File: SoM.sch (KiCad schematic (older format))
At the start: 9 parts

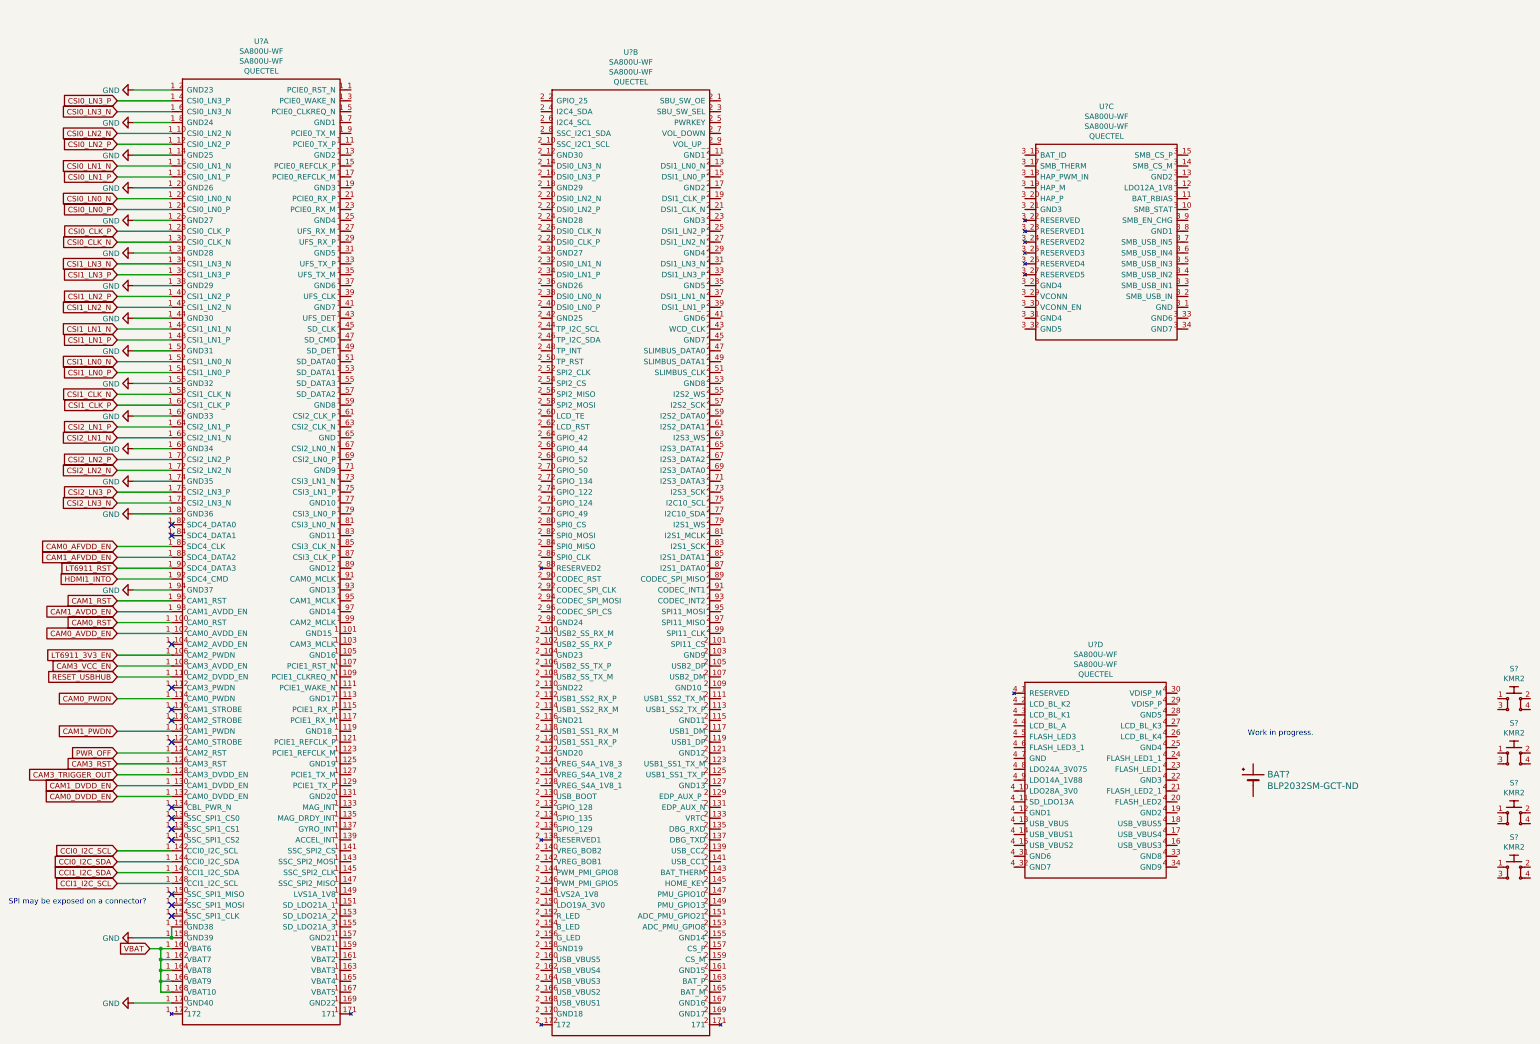
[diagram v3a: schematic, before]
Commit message: added components to pcb and fixed corresponding errors
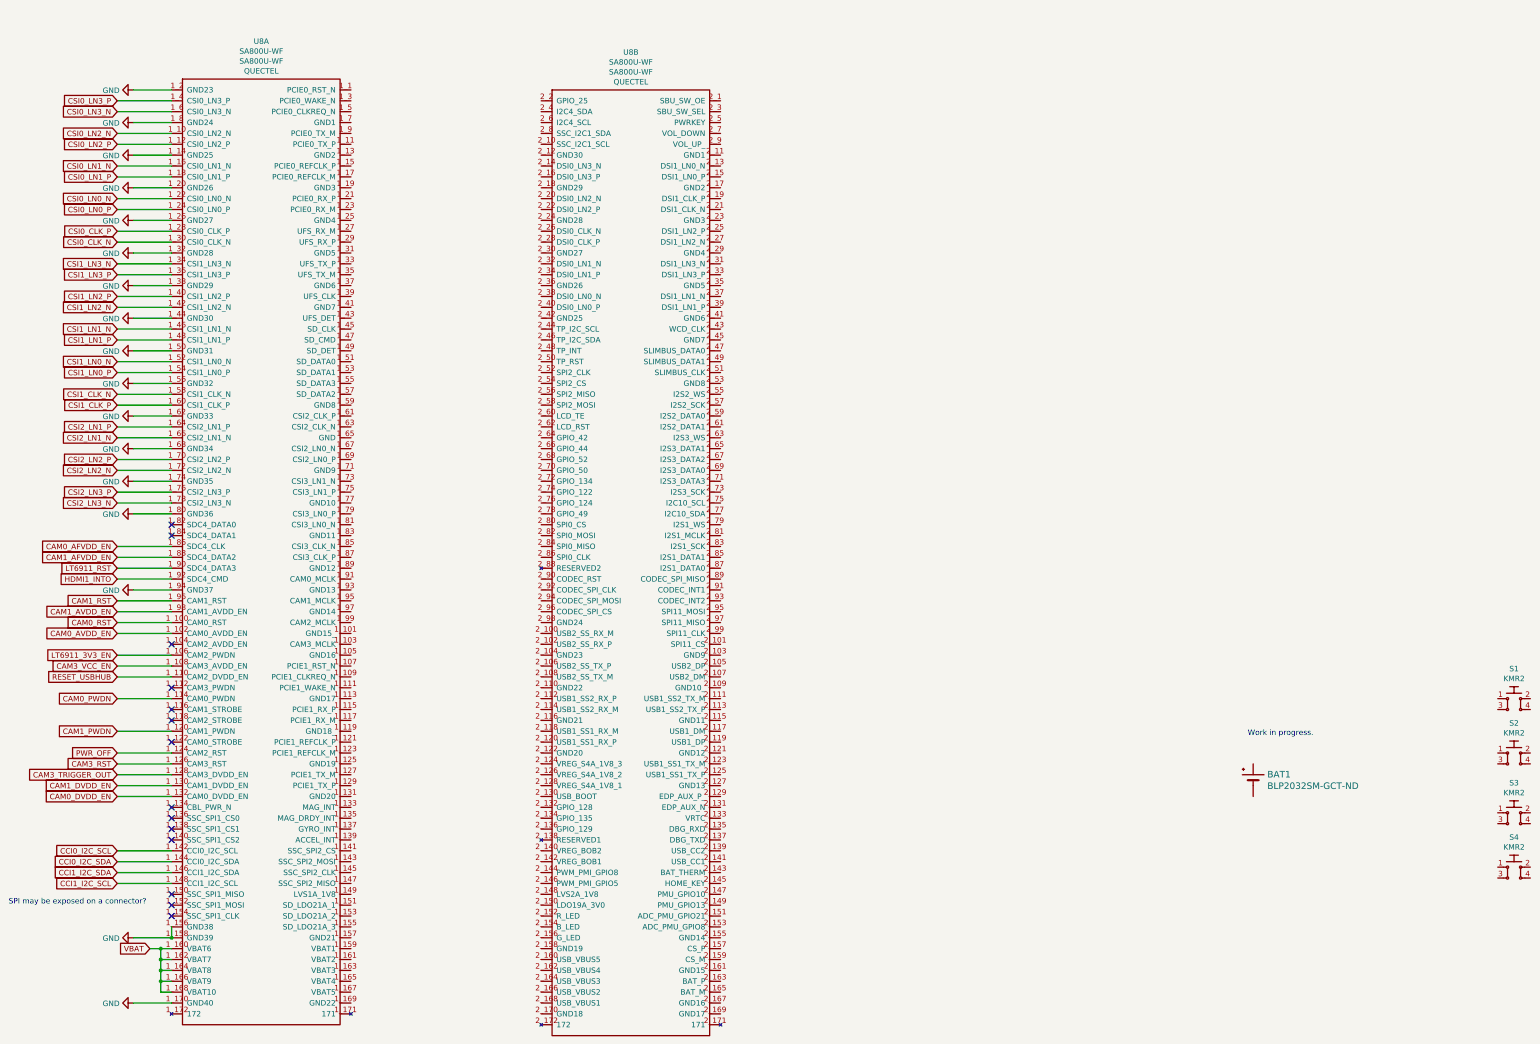
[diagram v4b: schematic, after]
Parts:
- removed U? (x2): SA800U-WF, antmicro-footprints:SA800U-WF, symbol antmicroMicrocontrollers:SA800U-WF
- gave numbers to parts that had none: 6
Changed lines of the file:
@@
 $EndDescr
 $Comp
-L power:GND #PWR?
+L power:GND #PWR037
 U 1 1 61AB272F
 P 1300 1750
-F 0 "#PWR?" H 1300 1500 50  0001 C CNN
+F 0 "#PWR037" H 1300 1500 50  0001 C CNN
 F 1 "GND" V 1305 1622 50  0000 R CNN
 F 2 "" H 1300 1750 50  0001 C CNN
@@
 CSI0_LN2_N
 $Comp
-L power:GND #PWR?
+L power:GND #PWR038
 U 1 1 61AB4B99
 P 1300 2050
-F 0 "#PWR?" H 1300 1800 50  0001 C CNN
+F 0 "#PWR038" H 1300 1800 50  0001 C CNN
 F 1 "GND" V 1305 1922 50  0000 R CNN
 F 2 "" H 1300 2050 50  0001 C CNN
@@
 	1150 2550 1650 2550
 $Comp
-L power:GND #PWR?
+L power:GND #PWR039
 U 1 1 61ABB2A4
 P 1300 2350
-F 0 "#PWR?" H 1300 2100 50  0001 C CNN
+F 0 "#PWR039" H 1300 2100 50  0001 C CNN
 F 1 "GND" V 1305 2222 50  0000 R CNN
 F 2 "" H 1300 2350 50  0001 C CNN
@@
 	1300 2350 1650 2350
 $Comp
-L power:GND #PWR?
+L power:GND #PWR040
 U 1 1 61ABBE0B
 P 1300 2650
-F 0 "#PWR?" H 1300 2400 50  0001 C CNN
+F 0 "#PWR040" H 1300 2400 50  0001 C CNN
 F 1 "GND" V 1305 2522 50  0000 R CNN
 F 2 "" H 1300 2650 50  0001 C CNN
@@
 CSI0_LN0_P
 $Comp
-L power:GND #PWR?
+L power:GND #PWR041
 U 1 1 61ABF0B1
 P 1300 2950
-F 0 "#PWR?" H 1300 2700 50  0001 C CNN
+F 0 "#PWR041" H 1300 2700 50  0001 C CNN
 F 1 "GND" V 1305 2822 50  0000 R CNN
 F 2 "" H 1300 2950 50  0001 C CNN
@@
 	1150 3150 1650 3150
 $Comp
-L power:GND #PWR?
+L power:GND #PWR042
 U 1 1 61AC25AA
 P 1300 3250
-F 0 "#PWR?" H 1300 3000 50  0001 C CNN
+F 0 "#PWR042" H 1300 3000 50  0001 C CNN
 F 1 "GND" V 1305 3122 50  0000 R CNN
 F 2 "" H 1300 3250 50  0001 C CNN
@@
 	1150 3450 1650 3450
 $Comp
-L power:GND #PWR?
+L power:GND #PWR043
 U 1 1 61AC444F
 P 1300 3550
-F 0 "#PWR?" H 1300 3300 50  0001 C CNN
+F 0 "#PWR043" H 1300 3300 50  0001 C CNN
 F 1 "GND" V 1305 3422 50  0000 R CNN
 F 2 "" H 1300 3550 50  0001 C CNN
@@
 CSI1_LN1_P
 $Comp
-L power:GND #PWR?
+L power:GND #PWR044
 U 1 1 61AC725F
 P 1300 3850
-F 0 "#PWR?" H 1300 3600 50  0001 C CNN
+F 0 "#PWR044" H 1300 3600 50  0001 C CNN
 F 1 "GND" V 1305 3722 50  0000 R CNN
 F 2 "" H 1300 3850 50  0001 C CNN
@@
 	1650 4150 1300 4150
 $Comp
-L power:GND #PWR?
+L power:GND #PWR045
 U 1 1 61AC9405
 P 1300 4150
-F 0 "#PWR?" H 1300 3900 50  0001 C CNN
+F 0 "#PWR045" H 1300 3900 50  0001 C CNN
 F 1 "GND" V 1305 4022 50  0000 R CNN
 F 2 "" H 1300 4150 50  0001 C CNN
@@
 	1650 4450 1300 4450
 $Comp
-L power:GND #PWR?
+L power:GND #PWR046
 U 1 1 61ACB8A4
 P 1300 4450
-F 0 "#PWR?" H 1300 4200 50  0001 C CNN
+F 0 "#PWR046" H 1300 4200 50  0001 C CNN
 F 1 "GND" V 1305 4322 50  0000 R CNN
 F 2 "" H 1300 4450 50  0001 C CNN
@@
 	1650 4750 1300 4750
 $Comp
-L power:GND #PWR?
+L power:GND #PWR047
 U 1 1 61ACE42A
 P 1300 4750
-F 0 "#PWR?" H 1300 4500 50  0001 C CNN
+F 0 "#PWR047" H 1300 4500 50  0001 C CNN
 F 1 "GND" V 1305 4622 50  0000 R CNN
 F 2 "" H 1300 4750 50  0001 C CNN
@@
 	1150 4950 1650 4950
 $Comp
-L power:GND #PWR?
+L power:GND #PWR048
 U 1 1 61AD13DC
 P 1300 5050
-F 0 "#PWR?" H 1300 4800 50  0001 C CNN
+F 0 "#PWR048" H 1300 4800 50  0001 C CNN
 F 1 "GND" V 1305 4922 50  0000 R CNN
 F 2 "" H 1300 5050 50  0001 C CNN
@@
 	1650 5350 1300 5350
 $Comp
-L power:GND #PWR?
+L power:GND #PWR049
 U 1 1 61AD5D86
 P 1300 5350
-F 0 "#PWR?" H 1300 5100 50  0001 C CNN
+F 0 "#PWR049" H 1300 5100 50  0001 C CNN
 F 1 "GND" V 1305 5222 50  0000 R CNN
 F 2 "" H 1300 5350 50  0001 C CNN
@@
 CSI2_LN3_N
 $Comp
-L power:GND #PWR?
+L power:GND #PWR050
 U 1 1 61AD8A80
 P 1300 5650
-F 0 "#PWR?" H 1300 5400 50  0001 C CNN
+F 0 "#PWR050" H 1300 5400 50  0001 C CNN
 F 1 "GND" V 1305 5522 50  0000 R CNN
 F 2 "" H 1300 5650 50  0001 C CNN
@@
 	1150 6250 1650 6250
 $Comp
-L power:GND #PWR?
+L power:GND #PWR051
 U 1 1 61AE7140
 P 1300 6350
-F 0 "#PWR?" H 1300 6100 50  0001 C CNN
+F 0 "#PWR051" H 1300 6100 50  0001 C CNN
 F 1 "GND" V 1305 6222 50  0000 R CNN
 F 2 "" H 1300 6350 50  0001 C CNN
@@
 	1650 9450 1650 9550
 $Comp
-L power:GND #PWR?
+L power:GND #PWR052
 U 1 1 61B400BB
 P 1300 9550
-F 0 "#PWR?" H 1300 9300 50  0001 C CNN
+F 0 "#PWR052" H 1300 9300 50  0001 C CNN
 F 1 "GND" V 1305 9422 50  0000 R CNN
 F 2 "" H 1300 9550 50  0001 C CNN
@@
 VBAT
 $Comp
-L power:GND #PWR?
+L power:GND #PWR053
 U 1 1 61B58726
 P 1300 10150
-F 0 "#PWR?" H 1300 9900 50  0001 C CNN
+F 0 "#PWR053" H 1300 9900 50  0001 C CNN
 F 1 "GND" V 1305 10022 50  0000 R CNN
 F 2 "" H 1300 10150 50  0001 C CNN
@@
 	1300 10150 1650 10150
 $Comp
-L antmicroMicrocontrollers:SA800U-WF U?
+L antmicroMicrocontrollers:SA800U-WF U8
 U 1 1 61B940C3
 P 1750 1650
-F 0 "U?" H 2475 1997 50  0000 C CNN
+F 0 "U8" H 2475 1997 50  0000 C CNN
 F 1 "SA800U-WF" H 2475 1906 50  0000 C CNN
 F 2 "antmicro-footprints:SA800U-WF" H 1750 1650 50  0001 C CNN
@@
 Connection ~ 1650 9550
 $Comp
-L antmicroMicrocontrollers:SA800U-WF U?
+L antmicroMicrocontrollers:SA800U-WF U8
 U 2 1 61BAF70E
 P 5150 1750
-F 0 "U?" H 5875 2097 50  0000 C CNN
+F 0 "U8" H 5875 2097 50  0000 C CNN
 F 1 "SA800U-WF" H 5875 2006 50  0000 C CNN
 F 2 "antmicro-footprints:SA800U-WF" H 5150 1750 50  0001 C CNN
@@
 $EndComp
 $Comp
-L antmicroMicrocontrollers:SA800U-WF U?
-U 3 1 61BB5D93
-P 9600 2250
-F 0 "U?" H 10250 2597 50  0000 C CNN
-F 1 "SA800U-WF" H 10250 2506 50  0000 C CNN
-F 2 "antmicro-footprints:SA800U-WF" H 9600 2250 50  0001 C CNN
-F 3 "https://www.quectel.com/wp-content/uploads/2021/05/Quectel_SA800U-WF_Hardware_Design_V1.0.pdf" H 9600 2250 50  0001 C CNN
-F 4 "SA800U-WF" H 10250 2415 50  0000 C CNN "MPN"
-F 5 "QUECTEL" H 10250 2324 50  0000 C CNN "Manufacturer"
-	3    9600 2250
-	1    0    0    -1
-$EndComp
-$Comp
-L antmicroMicrocontrollers:SA800U-WF U?
-U 4 1 61BBA563
-P 9500 7200
-F 0 "U?" H 10150 7547 50  0000 C CNN
-F 1 "SA800U-WF" H 10150 7456 50  0000 C CNN
-F 2 "antmicro-footprints:SA800U-WF" H 9500 7200 50  0001 C CNN
-F 3 "https://www.quectel.com/wp-content/uploads/2021/05/Quectel_SA800U-WF_Hardware_Design_V1.0.pdf" H 9500 7200 50  0001 C CNN
-F 4 "SA800U-WF" H 10150 7365 50  0000 C CNN "MPN"
-F 5 "QUECTEL" H 10150 7274 50  0000 C CNN "Manufacturer"
-	4    9500 7200
-	1    0    0    -1
-$EndComp
-$Comp
 L antmicroBatteryHoldersClipsContacts:BLP2032SM-GCT-ND BAT?
 U 1 1 61C092A2
 P 11600 8050
 AR Path="/61C092A2" Ref="BAT?"  Part="1"
-AR Path="/61A4BC4F/61C092A2" Ref="BAT?"  Part="1"
-F 0 "BAT?" H 11730 8053 60  0000 L CNN
+AR Path="/61A4BC4F/61C092A2" Ref="BAT1"  Part="1"
+F 0 "BAT1" H 11730 8053 60  0000 L CNN
 F 1 "BLP2032SM-GCT-ND" H 11730 7947 60  0000 L CNN
 F 2 "antmicro-footprints:BLP2032SM-GCT-ND" H 11600 8050 60  0001 C CNN
@@
 Work in progress.
 $Comp
-L antmicroPushbuttonSwitches:KMR2 S?
+L antmicroPushbuttonSwitches:KMR2 S1
 U 1 1 61C94E75
 P 14000 7350
-F 0 "S?" H 14000 7625 50  0000 C CNN
+F 0 "S1" H 14000 7625 50  0000 C CNN
 F 1 "KMR2" H 14000 7534 50  0000 C CNN
 F 2 "antmicro-footprints:SW_SPST_4.2x2.8" H 14200 7550 50  0001 L CNN
@@
 $EndComp
 $Comp
-L antmicroPushbuttonSwitches:KMR2 S?
+L antmicroPushbuttonSwitches:KMR2 S2
 U 1 1 61CA28EE
 P 14000 7850
-F 0 "S?" H 14000 8125 50  0000 C CNN
+F 0 "S2" H 14000 8125 50  0000 C CNN
 F 1 "KMR2" H 14000 8034 50  0000 C CNN
 F 2 "antmicro-footprints:SW_SPST_4.2x2.8" H 14200 8050 50  0001 L CNN
@@
 $EndComp
 $Comp
-L antmicroPushbuttonSwitches:KMR2 S?
+L antmicroPushbuttonSwitches:KMR2 S3
 U 1 1 61CA563B
 P 14000 8400
-F 0 "S?" H 14000 8675 50  0000 C CNN
+F 0 "S3" H 14000 8675 50  0000 C CNN
 F 1 "KMR2" H 14000 8584 50  0000 C CNN
 F 2 "antmicro-footprints:SW_SPST_4.2x2.8" H 14200 8600 50  0001 L CNN
@@
 $EndComp
 $Comp
-L antmicroPushbuttonSwitches:KMR2 S?
+L antmicroPushbuttonSwitches:KMR2 S4
 U 1 1 61CA8515
 P 14000 8900
-F 0 "S?" H 14000 9175 50  0000 C CNN
+F 0 "S4" H 14000 9175 50  0000 C CNN
 F 1 "KMR2" H 14000 9084 50  0000 C CNN
 F 2 "antmicro-footprints:SW_SPST_4.2x2.8" H 14200 9100 50  0001 L CNN

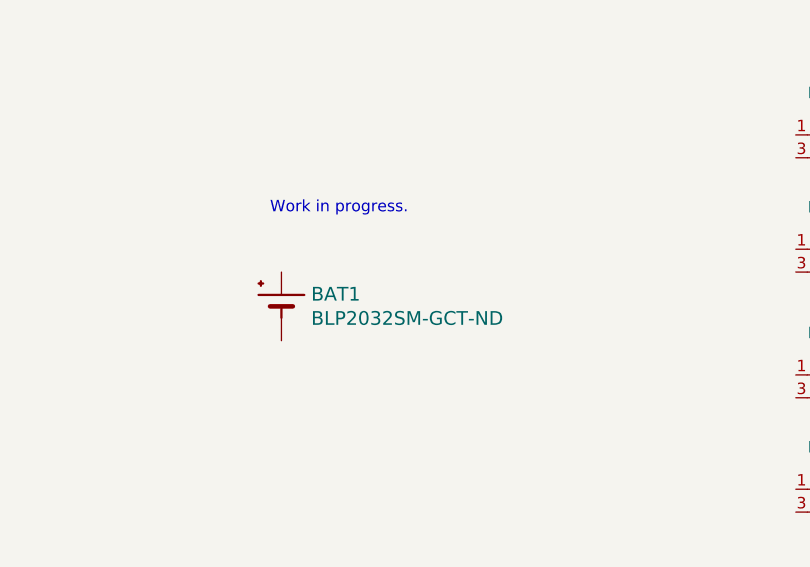
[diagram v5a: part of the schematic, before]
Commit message: changed rtc battery to smaller model
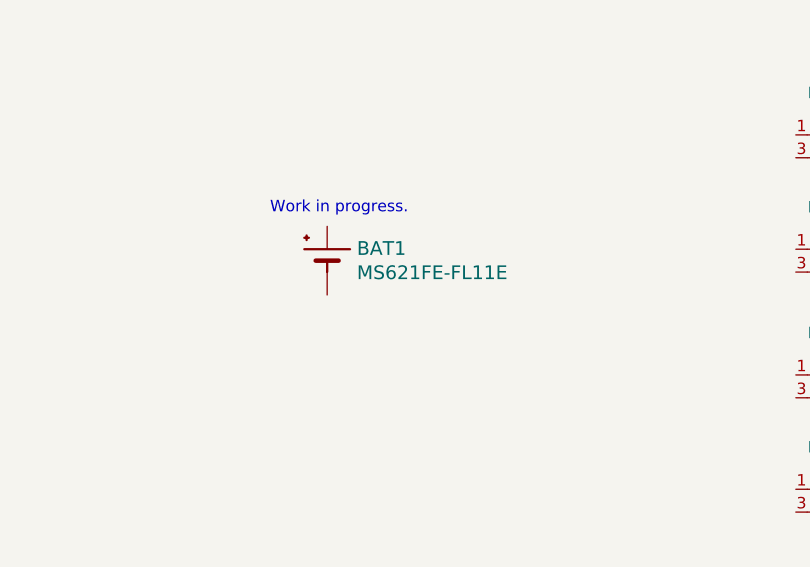
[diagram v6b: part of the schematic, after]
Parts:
- removed BAT1: BLP2032SM-GCT-ND, antmicro-footprints:BLP2032SM-GCT-ND, symbol antmicroBatteryHoldersClipsContacts:BLP2032SM-GCT-ND
- added BAT1: MS621FE-FL11E, antmicro-footprints:MS621FE-FL11E, symbol antmicroBatteryHoldersClipsContacts:MS621FE-FL11E
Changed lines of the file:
@@
-	1    0    0    -1
-$EndComp
-$Comp
-L antmicroBatteryHoldersClipsContacts:BLP2032SM-GCT-ND BAT?
-U 1 1 61C092A2
-P 11600 8050
-AR Path="/61C092A2" Ref="BAT?"  Part="1"
-AR Path="/61A4BC4F/61C092A2" Ref="BAT1"  Part="1"
-F 0 "BAT1" H 11730 8053 60  0000 L CNN
-F 1 "BLP2032SM-GCT-ND" H 11730 7947 60  0000 L CNN
-F 2 "antmicro-footprints:BLP2032SM-GCT-ND" H 11600 8050 60  0001 C CNN
-F 3 "" H 11600 8050 60  0001 C CNN
-F 4 "MPD" H 11600 8050 50  0001 C CNN "Manufacturer"
-F 5 "BLP2032SM-GCT-ND" H 11600 8050 50  0001 C CNN "MPN"
-	1    11600 8050
 	1    0    0    -1
 $EndComp
@@
 	1    0    0    -1
 $EndComp
+$Comp
+L antmicroBatteryHoldersClipsContacts:MS621FE-FL11E BAT1
+U 1 1 61B43805
+P 11800 7850
+F 0 "BAT1" H 11930 7853 60  0000 L CNN
+F 1 "MS621FE-FL11E" H 11930 7747 60  0000 L CNN
+F 2 "antmicro-footprints:MS621FE-FL11E" H 11800 7850 60  0001 C CNN
+F 3 "" H 11800 7850 60  0001 C CNN
+F 4 "Seiko" H 11800 7850 50  0001 C CNN "Manufacturer"
+F 5 "MS621FE-FL11E" H 11800 7850 50  0001 C CNN "MPN"
+	1    11800 7850
+	1    0    0    -1
+$EndComp
